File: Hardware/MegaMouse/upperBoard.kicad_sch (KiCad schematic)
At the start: 24 parts, among them J601 USBC, U601 FT232RL, U602 SN74HC595, U603 STATE

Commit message: Bump config
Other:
- company: SNHU -> Kitsune Scientific
- title: Inverted Pendulum Controller -> MegaMouse
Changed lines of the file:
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@@
   (paper "A4")
   (title_block
-    (title "Inverted Pendulum Controller")
+    (title "MegaMouse")
     (date "${ISSUE}")
     (rev "${REVISION}")
-    (company "SNHU")
+    (company "Kitsune Scientific")
     (comment 4 "Release: ${FULL_REVISION}")
   )

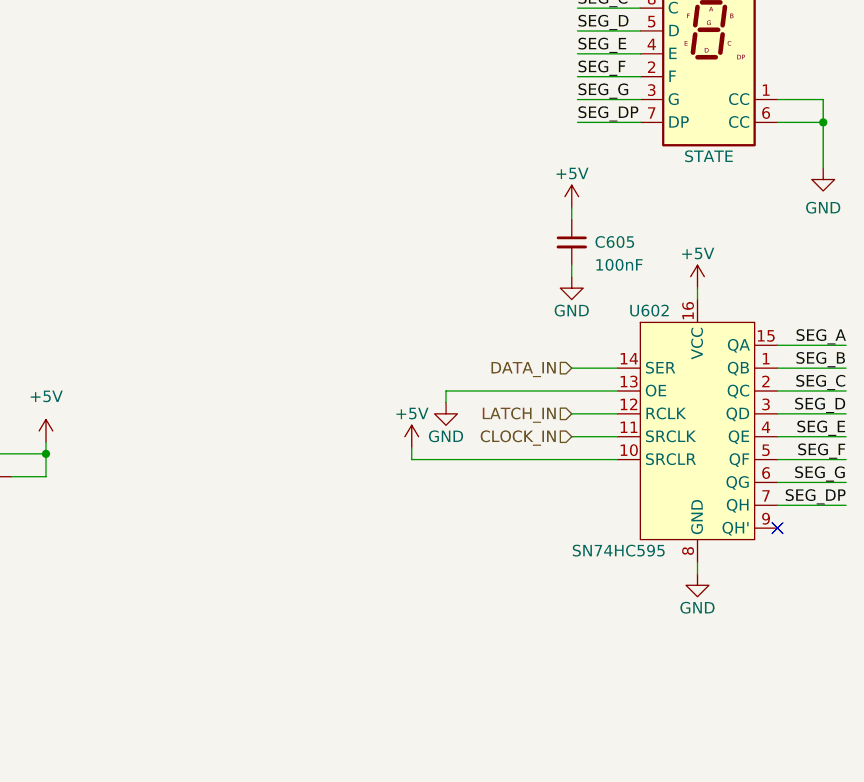
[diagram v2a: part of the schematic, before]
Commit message: Add IR sensor
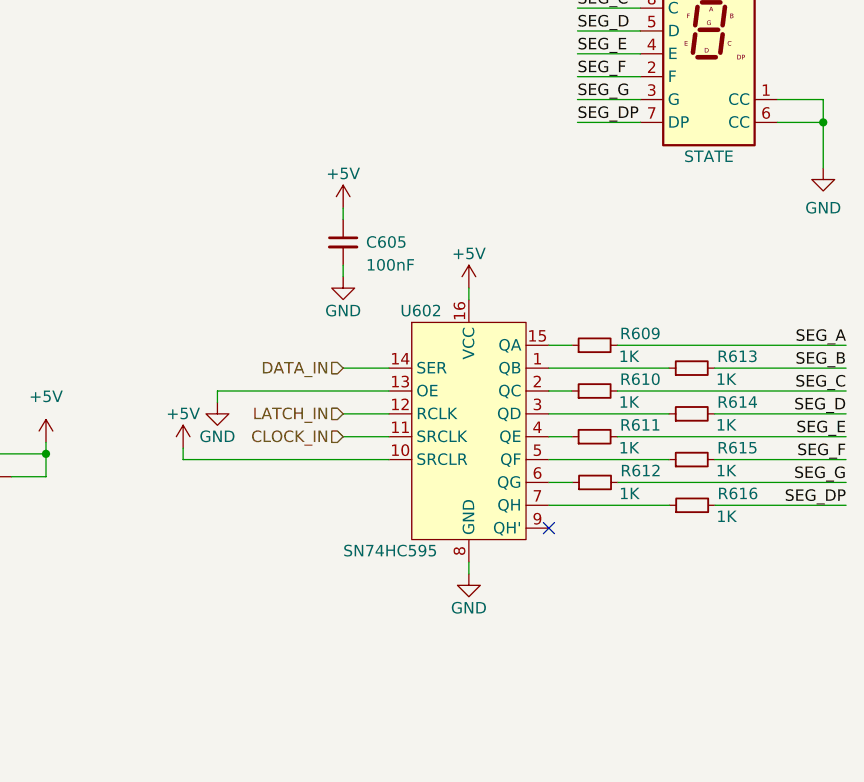
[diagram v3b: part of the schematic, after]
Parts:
- added R609, R610, R611, R612, R613, R614, R615, R616: 1K, Resistor_SMD:R_0805_2012Metric, symbol Device:R_Small
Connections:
- net SEG_A: now also R609.2; no longer U602.15 (QA)
- net SEG_B: now also R613.2; no longer U602.1 (QB)
- net SEG_C: now also R610.2; no longer U602.2 (QC)
- net SEG_D: now also R614.2; no longer U602.3 (QD)
- net SEG_DP: now also R616.2; no longer U602.7 (QH)
- net SEG_E: now also R611.2; no longer U602.4 (QE)
- net SEG_F: now also R615.2; no longer U602.5 (QF)
- net SEG_G: now also R612.2; no longer U602.6 (QG)
- new net: R613.1, U602.1 (QB)
- new net: R611.1, U602.4 (QE)
- new net: R609.1, U602.15 (QA)
- new net: R614.1, U602.3 (QD)
- new net: R610.1, U602.2 (QC)
- new net: R615.1, U602.5 (QF)
- new net: R612.1, U602.6 (QG)
- new net: R616.1, U602.7 (QH)
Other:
- moved on the sheet: C605, U602

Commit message: Verification 1 (#3)
And thats all we have time for folks.
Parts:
- removed U603: STATE, Display_7Segment:HDSP-7801, symbol Display_Character:HDSP-7803
- added U604: STATE, KenwoodFox:SM420391N8, symbol KenwoodFox:SM420391N
- U601: LCSC# (none) -> C8690
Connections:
- net GND: now also U604.3 (CA), U604.8 (CA)
- net SEG_A: now also U604.10 (A)
- net SEG_B: now also U604.9 (B)
- net SEG_C: now also U604.7 (C)
- net SEG_D: now also U604.5 (D)
- net SEG_DP: now also U604.6 (DP)
- net SEG_E: now also U604.4 (E)
- net SEG_F: now also U604.2 (F)
- net SEG_G: now also U604.1 (G)
